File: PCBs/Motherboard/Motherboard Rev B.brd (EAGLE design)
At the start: 95.9 x 90.2 mm, 29 parts, among them Q1 32kHZ, U1 Value, U2 TPS22942DCKR

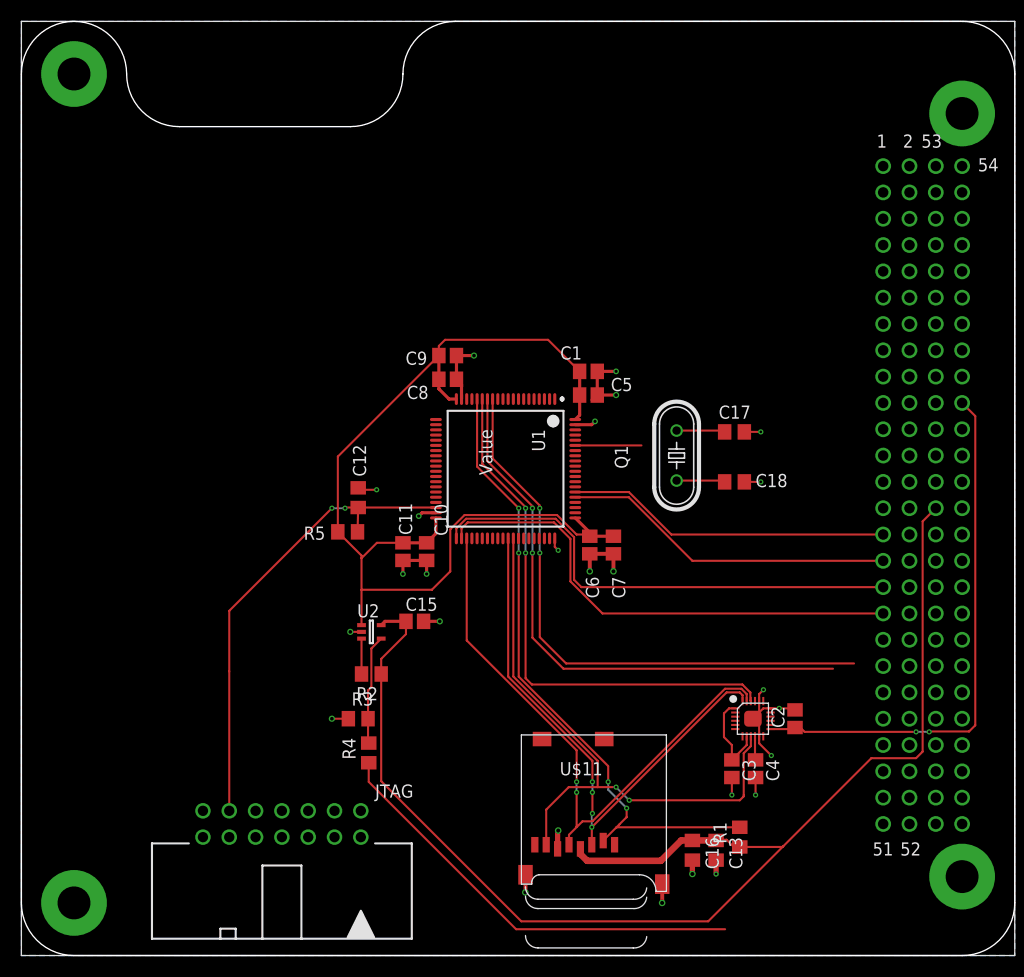
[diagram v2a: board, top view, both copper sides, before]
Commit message: Use common PC104 footprint with dimensions set per board
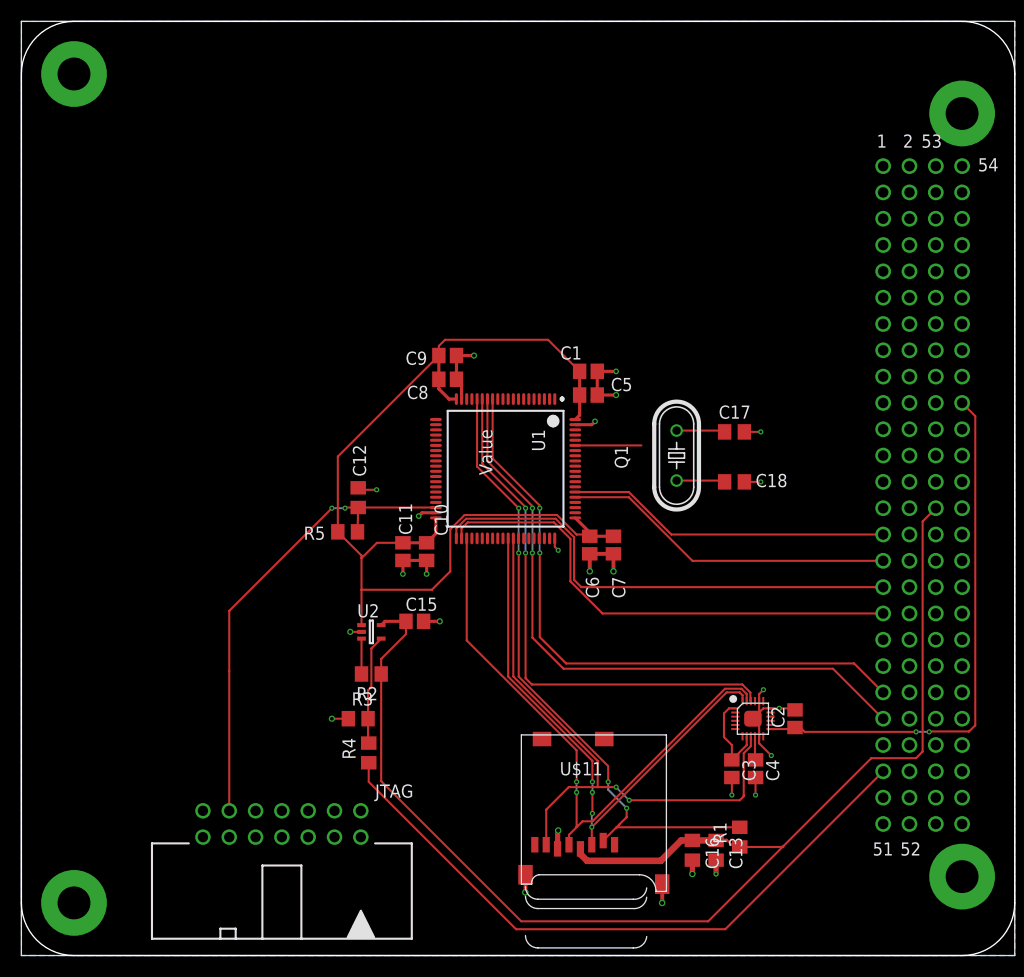
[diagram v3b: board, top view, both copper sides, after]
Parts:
- U$1: value PC104_MOBO -> PC104_NO_DIMENSION; device Cubesat:PC104_MOBO -> Cubesat:PC104_NO_DIMENSION
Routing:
- net LI_OA_RESET: track 42.1 -> 63.7 mm
- net SCL: track 55.1 -> 61.9 mm
- net SDA: track 56.3 -> 60.2 mm
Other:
- outline, holes or cut-outs redrawn
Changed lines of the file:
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@@
 <board>
 <plain>
+<wire x1="0" y1="85.09" x2="0" y2="5.08" width="0.127" layer="20"/>
+<wire x1="0" y1="5.08" x2="5.08" y2="0" width="0.127" layer="20" curve="90"/>
+<wire x1="5.08" y1="0" x2="90.805" y2="0" width="0.127" layer="20"/>
+<wire x1="90.805" y1="0" x2="95.885" y2="5.08" width="0.127" layer="20" curve="90"/>
+<wire x1="95.885" y1="5.08" x2="95.885" y2="85.09" width="0.127" layer="20"/>
+<wire x1="95.885" y1="85.09" x2="90.678" y2="90.17" width="0.127" layer="20" curve="91.414625"/>
+<wire x1="0" y1="85.09" x2="5.08" y2="90.17" width="0.127" layer="20" curve="-90"/>
+<wire x1="5.08" y1="90.17" x2="90.678" y2="90.17" width="0.127" layer="20"/>
 </plain>
 <attributes>
@@
 <element name="R3" library="resistor" library_urn="urn:adsk.eagle:library:348" package="R0805" package3d_urn="urn:adsk.eagle:package:23553/2" value="100k" x="32.512" y="22.86"/>
 <element name="R4" library="resistor" library_urn="urn:adsk.eagle:library:348" package="R0805" package3d_urn="urn:adsk.eagle:package:23553/2" value="0" x="33.528" y="19.558" rot="R90"/>
-<element name="U$1" library="Cubesat" package="PC104_MOBO" value="PC104_MOBO" x="0" y="0"/>
+<element name="U$1" library="Cubesat" package="PC104_NO_DIMENSION" value="PC104_NO_DIMENSION" x="0" y="0"/>
 </elements>
 <signals>
@@
 <via x="50.038" y="43.18" extent="1-16" drill="0.254"/>
 <wire x1="45.486" y1="47.986" x2="45.486" y2="53.715" width="0.2032" layer="1"/>
-<wire x1="80.37321875" y1="28.194" x2="52.578" y2="28.194" width="0.2032" layer="1"/>
+<wire x1="52.578" y1="28.194" x2="80.37321875" y2="28.194" width="0.2032" layer="1"/>
 <wire x1="52.578" y1="28.194" x2="50.038" y2="30.734" width="0.2032" layer="1"/>
 <wire x1="50.038" y1="43.434" x2="45.486" y2="47.986" width="0.2032" layer="1"/>
 <wire x1="50.038" y1="43.18" x2="50.038" y2="43.434" width="0.2032" layer="1"/>
 <contactref element="U$1" pad="41"/>
-<wire x1="83.185" y1="25.4" x2="80.37321875" y2="28.194" width="0" layer="19" extent="1-1"/>
+<wire x1="80.37321875" y1="28.194" x2="83.16721875" y2="25.4" width="0.2032" layer="1"/>
+<wire x1="83.16721875" y1="25.4" x2="83.185" y2="25.4" width="0.2032" layer="1"/>
 </signal>
 <signal name="SCL">
 <contactref element="U1" pad="14"/>
-<wire x1="78.34121875" y1="27.686" x2="52.324" y2="27.686" width="0.2032" layer="1"/>
+<wire x1="52.324" y1="27.686" x2="78.34121875" y2="27.686" width="0.2032" layer="1"/>
 <wire x1="52.324" y1="27.686" x2="49.3268" y2="30.6832" width="0.2032" layer="1"/>
 <wire x1="49.3268" y1="30.6832" x2="49.3268" y2="38.862" width="0.2032" layer="1"/>
@@
 <wire x1="49.3268" y1="43.18" x2="49.3268" y2="43.3832" width="0.2032" layer="1"/>
 <contactref element="U$1" pad="43"/>
-<wire x1="83.185" y1="22.86" x2="78.34121875" y2="27.686" width="0" layer="19" extent="1-1"/>
+<wire x1="78.34121875" y1="27.686" x2="83.16721875" y2="22.86" width="0.2032" layer="1"/>
+<wire x1="83.16721875" y1="22.86" x2="83.185" y2="22.86" width="0.2032" layer="1"/>
 </signal>
 <signal name="MOSI">
@@
 <contactref element="U1" pad="42"/>
 <wire x1="52.9964" y1="36.116475" x2="52.9964" y2="40.2216" width="0.2032" layer="1"/>
-<wire x1="56.092875" y1="33.02" x2="52.9964" y2="36.116475" width="0.2032" layer="1"/>
+<wire x1="52.9964" y1="36.116475" x2="56.092875" y2="33.02" width="0.2032" layer="1"/>
 <wire x1="52.9964" y1="40.2216" x2="51.4096" y2="41.8084" width="0.2032" layer="1"/>
 <wire x1="42.486" y1="41.216" x2="42.486" y2="40.265" width="0.2032" layer="1"/>
@@
 <wire x1="43.0784" y1="41.8084" x2="42.486" y2="41.216" width="0.2032" layer="1"/>
 <contactref element="U$1" pad="35"/>
-<wire x1="83.185" y1="33.02" x2="56.092875" y2="33.02" width="0.2032" layer="1"/>
+<wire x1="56.092875" y1="33.02" x2="83.185" y2="33.02" width="0.2032" layer="1"/>
 </signal>
 <signal name="PINAVL1_TX">
@@
 <wire x1="53.352" y1="40.374" x2="51.562" y2="42.164" width="0.2032" layer="1"/>
 <wire x1="53.352" y1="36.263775" x2="53.352" y2="40.374" width="0.2032" layer="1"/>
-<wire x1="54.055775" y1="35.56" x2="53.352" y2="36.263775" width="0.2032" layer="1"/>
+<wire x1="53.352" y1="36.263775" x2="54.055775" y2="35.56" width="0.2032" layer="1"/>
 <wire x1="51.562" y1="42.164" x2="42.926" y2="42.164" width="0.2032" layer="1"/>
 <wire x1="41.986" y1="41.224" x2="41.986" y2="40.265" width="0.2032" layer="1"/>
 <wire x1="42.926" y1="42.164" x2="41.986" y2="41.224" width="0.2032" layer="1"/>
 <contactref element="U$1" pad="33"/>
-<wire x1="83.185" y1="35.56" x2="54.055775" y2="35.56" width="0.2032" layer="1"/>
+<wire x1="54.055775" y1="35.56" x2="83.185" y2="35.56" width="0.2032" layer="1"/>
 </signal>
 <signal name="LITHIUM_RX">
 <contactref element="U1" pad="66"/>
 <wire x1="58.638" y1="44.74" x2="53.461" y2="44.74" width="0.2032" layer="1"/>
-<wire x1="62.738" y1="40.64" x2="58.638" y2="44.74" width="0.2032" layer="1"/>
+<wire x1="58.638" y1="44.74" x2="62.738" y2="40.64" width="0.2032" layer="1"/>
 <contactref element="U$1" pad="29"/>
-<wire x1="83.185" y1="40.64" x2="62.738" y2="40.64" width="0.2032" layer="1"/>
+<wire x1="62.738" y1="40.64" x2="83.185" y2="40.64" width="0.2032" layer="1"/>
 </signal>
 <signal name="LITHIUM_TX">
 <contactref element="U1" pad="65"/>
 <wire x1="58.63" y1="44.24" x2="53.461" y2="44.24" width="0.2032" layer="1"/>
-<wire x1="64.77" y1="38.1" x2="58.63" y2="44.24" width="0.2032" layer="1"/>
+<wire x1="58.63" y1="44.24" x2="64.77" y2="38.1" width="0.2032" layer="1"/>
 <contactref element="U$1" pad="31"/>
-<wire x1="83.185" y1="38.1" x2="64.77" y2="38.1" width="0.2032" layer="1"/>
+<wire x1="64.77" y1="38.1" x2="83.185" y2="38.1" width="0.2032" layer="1"/>
 </signal>
 <signal name="SW10">
@@
 <wire x1="86.36" y1="21.59" x2="75.604" y2="21.59" width="0.2032" layer="1"/>
 <wire x1="75.604" y1="21.59" x2="75.184" y2="22.01" width="0.2032" layer="1"/>
+<wire x1="92.075" y1="52.07" x2="92.075" y2="22.225" width="0.2032" layer="1"/>
 <contactref element="U$1" pad="72"/>
 <wire x1="90.805" y1="53.34" x2="92.075" y2="52.07" width="0.2032" layer="1"/>
-<wire x1="92.075" y1="52.07" x2="92.075" y2="22.225" width="0.2032" layer="1"/>
 <wire x1="70.012" y1="21.16" x2="72.312" y2="21.86" width="0" layer="19" extent="1-1"/>
 </signal>
@@
 </signal>
 <signal name="LI_OA_RESET">
-<wire x1="67.92721875" y1="2.54" x2="47.752" y2="2.54" width="0.2032" layer="1"/>
 <contactref element="R4" pad="1"/>
 <wire x1="33.528" y1="16.764" x2="33.528" y2="18.608" width="0.2032" layer="1"/>
 <wire x1="47.752" y1="2.54" x2="33.528" y2="16.764" width="0.2032" layer="1"/>
+<wire x1="47.752" y1="2.54" x2="67.945" y2="2.54" width="0.2032" layer="1"/>
 <contactref element="U$1" pad="47"/>
-<wire x1="83.185" y1="17.78" x2="67.92721875" y2="2.54" width="0" layer="19" extent="1-1"/>
+<wire x1="67.945" y1="2.54" x2="83.185" y2="17.78" width="0.2032" layer="1"/>
 </signal>
 <signal name="N$1">

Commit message: So. many. changes.
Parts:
- added C14: 10uF, adafruit:C0805
- added DF11: DF11-8DP-2DS(52), DF11:CON8_2X4_RF_DF11
- added J1: MOLEX_504050-0491, Molex 504050-0491:MOLEX_5040500491
- added JTAG_PWR: MOLEX_SL_03-87898, molex-sl-connectors_jw:SL_87898_3
- added LTC6081: LTC6081HMS8PBF, LTC6081:MSOP-8_MS
- added R10, R11, R17, R18, R19, R9: 350, resistor:R0805
- added R12, R20: 50, Bourns 3224J:3224J
- added R13, R14, R21, R22: 10k, resistor:R0805
- added R15, R16, R23, R24: 330k, resistor:R0805
- added R6, R8: 100k, resistor:R0805
- added R7: 0, resistor:R0805
- added U$3: FPF2105, FPF2105:SOT23-5
- C12: value 2.2nF -> 1nF
- renumbered U2 to TPS22942
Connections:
- removed net INT: U$2.12
- removed net N$4 (its old number): C18.1, Q1.1, U1.75
- removed net RST: C12.1, JTAG.11, R5.1, U1.38
- removed net TCK: JTAG.7, U1.24
- removed net TDI: JTAG.3, U1.22
- removed net TDO: JTAG.1, U1.21
- removed net TEST: JTAG.8, U1.37
- removed net TMS: JTAG.5, U1.23
- new net 3V1: C14.1
- new net 3V3_SD: C13.1, C16.1, R1.1, U$11.4, U$3.5
- new net EXT_RXD: JTAG.14, U1.36
- new net EXT_TXD: JTAG.12, U1.35
- new net INT_IMU: U$2.12, U1.44
- new net N$10: LTC6081.2, R14.2, R16.2
- new net N$11: R18.2, R19.1, R21.1
- new net N$12: LTC6081.5, R21.2, R23.2
- new net N$13: LTC6081.6, R22.2, R24.2
- new net N$2: R6.2, R7.2, U$3.3
- new net N$6: C18.1, Q1.1, U1.77
- new net N$7: R8.2, U$3.4
- new net N$8: R10.2, R11.1, R13.1
- new net N$9: LTC6081.3, R13.2, R15.2
- new net SBWTCK: JTAG.7, U1.37
- new net SBWTDIO: C12.1, JTAG.1, R5.1, U1.38
- new net STR1: LTC6081.1, R16.1, U1.5
- new net STR1_L1: DF11.1, R12.2
- new net STR1_L2: DF11.2, R9.2
- new net STR1_L3: DF11.3, R14.1
- new net STR2: LTC6081.7, R24.1, U1.6
- new net STR2_L1: DF11.4, R20.2
- new net STR2_L2: DF11.5, R17.2
- new net STR2_L3: DF11.6, R22.1
- new net SW5: J1.1, U$1.65
- new net TMP_L1: DF11.7
- new net TMP_L2: DF11.8
- new net VCC_TARGET: JTAG.4, JTAG_PWR.3
- new net VCC_TOOL: JTAG.2, JTAG_PWR.1
- net 3V3: now also R8.1, U$3.1; no longer C13.1, C16.1, R1.1, U$11.4
- net 3V3_UC: now also JTAG_PWR.2
- net CS_SD: now also U1.31; no longer U1.16
- net GND: now also C14.2, J1.4, J1.SH1, J1.SH2, LTC6081.4, R10.1, R15.1, R17.1, R18.1, R23.1, R6.1, R9.1, U$3.2
- net LI_OA_RESET: now also R7.1
- net SCL: now also J1.2
- net SDA: now also J1.3
- net SW10: now also LTC6081.8, R11.2, R12.1, R19.2, R20.1
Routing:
- net RST: track 45.7 -> 0.00 mm, vias 2 -> 0
- net 3V3: track 129.2 -> 107.7 mm
- net 3V3_UC: track 99.7 -> 114.4 mm
- net N$4 (its old number): track 11.1 -> 0.00 mm
- net SBWTDIO: track 0.00 -> 9.85 mm
- net N$4: track 4.79 -> 0.00 mm
- net GND: track 51.6 -> 48.4 mm, vias 23 -> 21
- net CS_SD: track 61.4 -> 58.7 mm
